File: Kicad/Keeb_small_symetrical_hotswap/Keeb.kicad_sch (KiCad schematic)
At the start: 19 parts, among them J1 MJ-4PP-9, SW10 CherryMX, SW11 CherryMX, SW13 CherryMX, SW14 CherryMX, SW15 CherryMX, SW16 CherryMX, SW17 CherryMX, SW18 CherryMX, SW19 CherryMX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

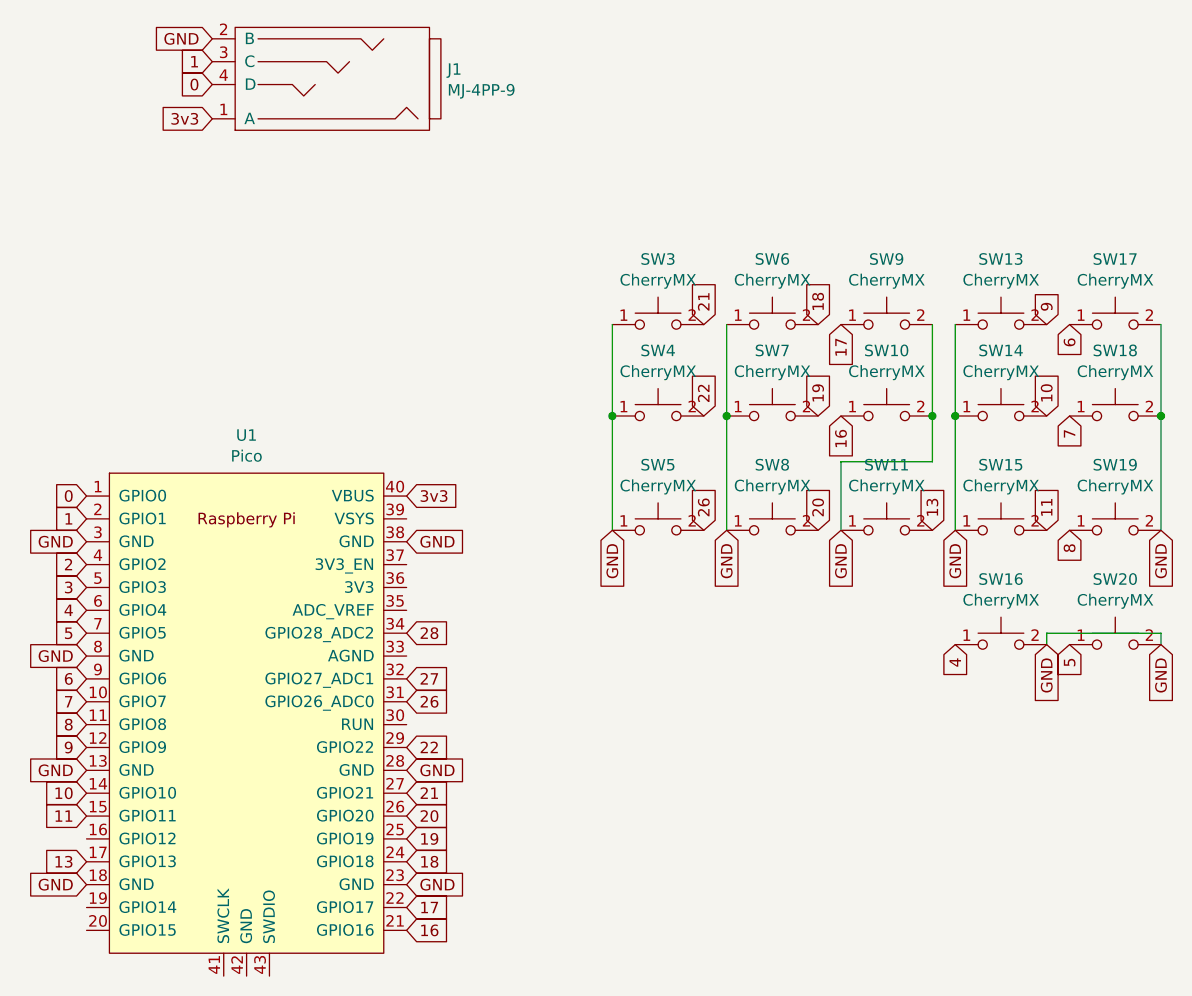
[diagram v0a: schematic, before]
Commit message: Added universal left-right pcb design, started work on hotswap variant
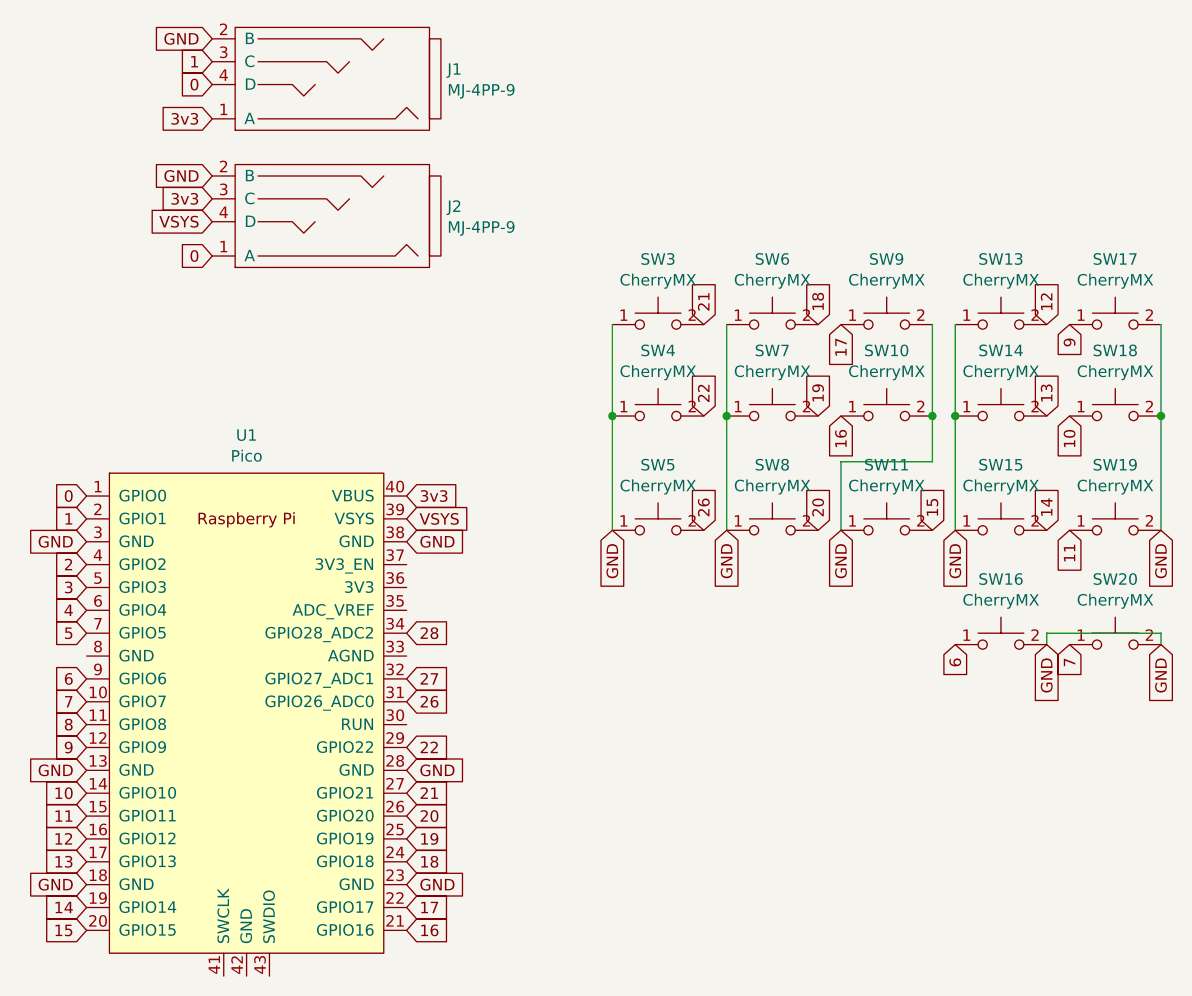
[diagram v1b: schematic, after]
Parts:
- added J2: MJ-4PP-9, MJ-4PP-9:MJ-4PP-9, symbol Keeb-rescue:MJ-4PP-9-MJ-4PP-9
- J1: footprint MJ-4PP-9:MJ-4PP-9_no_silk -> MJ-4PP-9:MJ-4PP-9
- SW10, SW11, SW13, SW14, SW15, SW16, SW17, SW18, SW19, SW20, SW3, SW4, SW5, SW6, SW7, SW8, SW9: footprint ScottoKeebs_MX:MX_PCB_1.00u -> ScottoKeebs_Hotswap:Hotswap_MX_1.00u
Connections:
- net 0: now also J2.1 (A)
- net 10: now also SW18.1; no longer SW14.2
- net 11: now also SW19.1; no longer SW15.2
- net 13: now also SW14.2; no longer SW11.2
- net 3v3: now also J2.3 (C)
- net 4: no longer SW16.1
- net 5: no longer SW20.1
- net 6: now also SW16.1; no longer SW17.1
- net 7: now also SW20.1; no longer SW18.1
- net 8: no longer SW19.1
- net 9: now also SW17.1; no longer SW13.2
- net GND: now also J2.2 (B); no longer U1.8 (GND)
- net 12: now reaches U1.16 (GPIO12)
- net 12: now also SW13.2
- net 14: now reaches U1.19 (GPIO14)
- net 14: now also SW15.2
- net 15: now reaches U1.20 (GPIO15)
- net 15: now also SW11.2
- net VSYS: now reaches U1.39 (VSYS)
- net VSYS: now also J2.4 (D)
